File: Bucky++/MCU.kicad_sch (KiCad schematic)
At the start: 38 parts, among them J15 502585-0470, J16 FTSH-105-01-F-D-RA-K, J1702 505110-3091, J1801 S2B-PH-SM4-TB, J403 USB4105-GF-A, Q1401 PMV90ENER, U1 STM32G483RET6, U1801 DGD0216WT-7, Y201 ABM8W-48.0000MHZ-4-D1X-T3

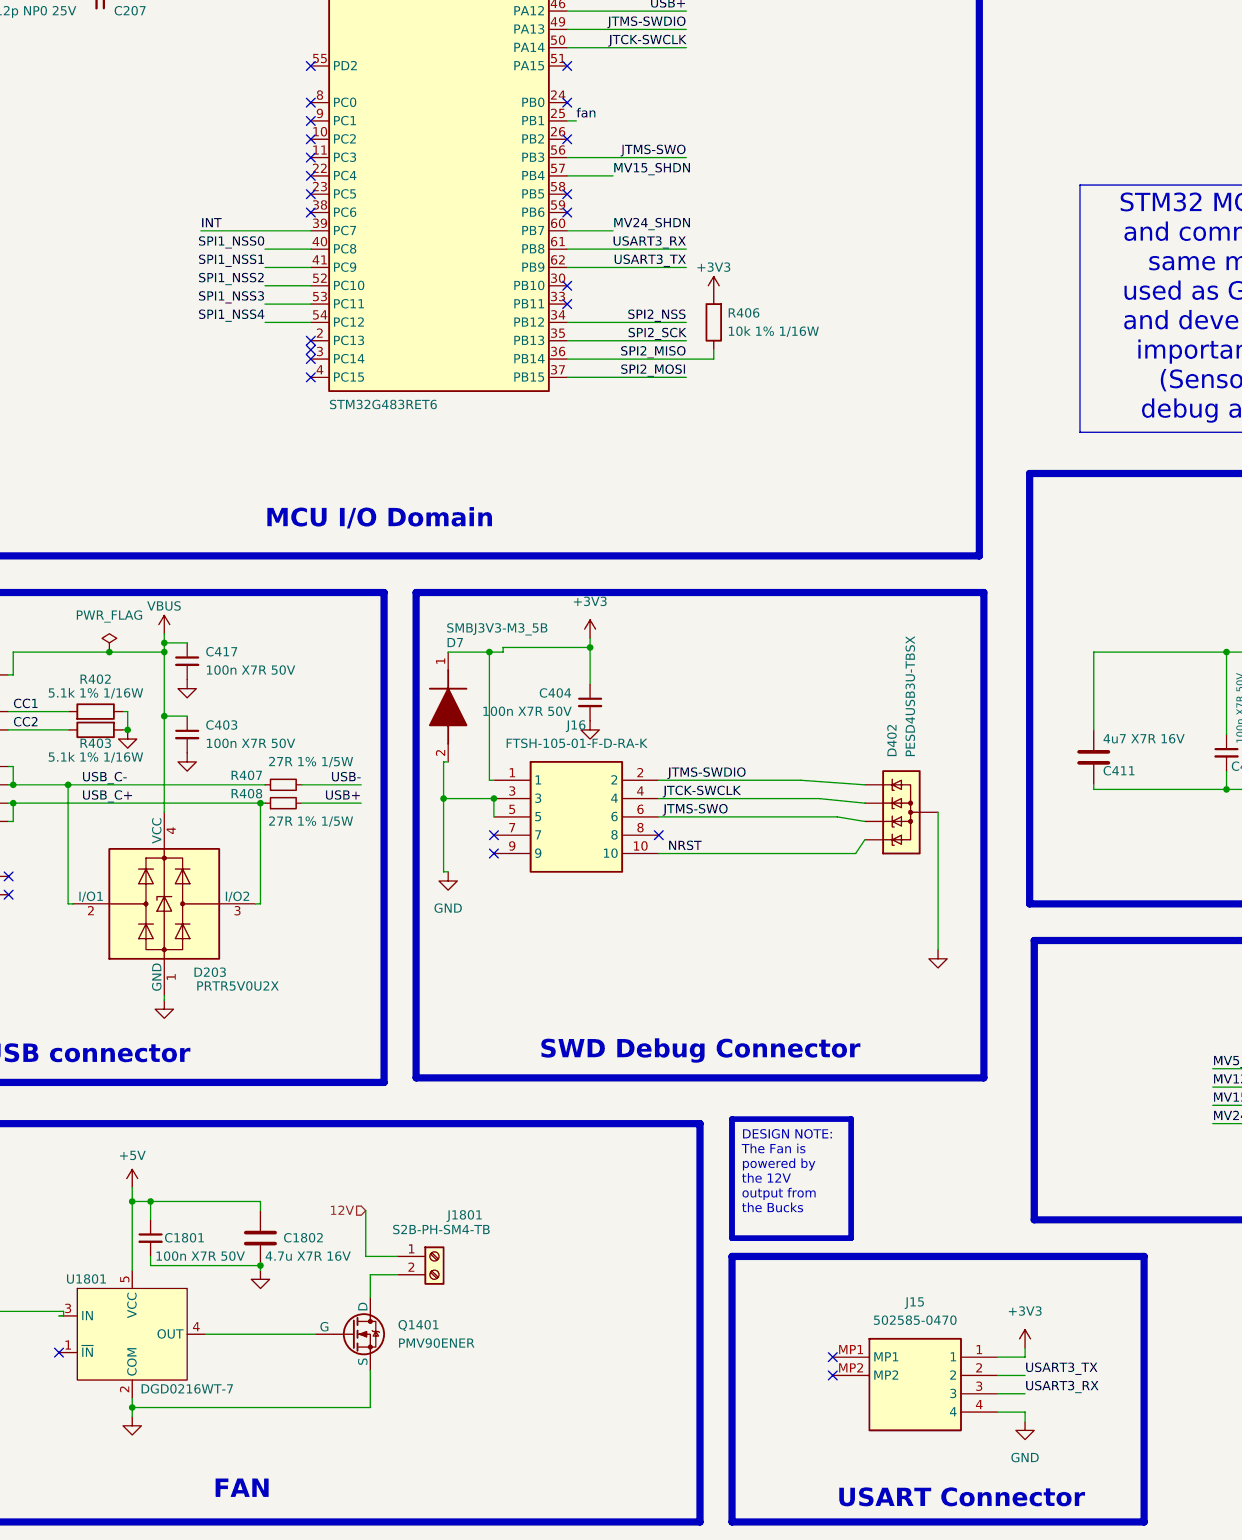
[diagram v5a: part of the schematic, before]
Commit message: updated circuit after review. updated silkscreen
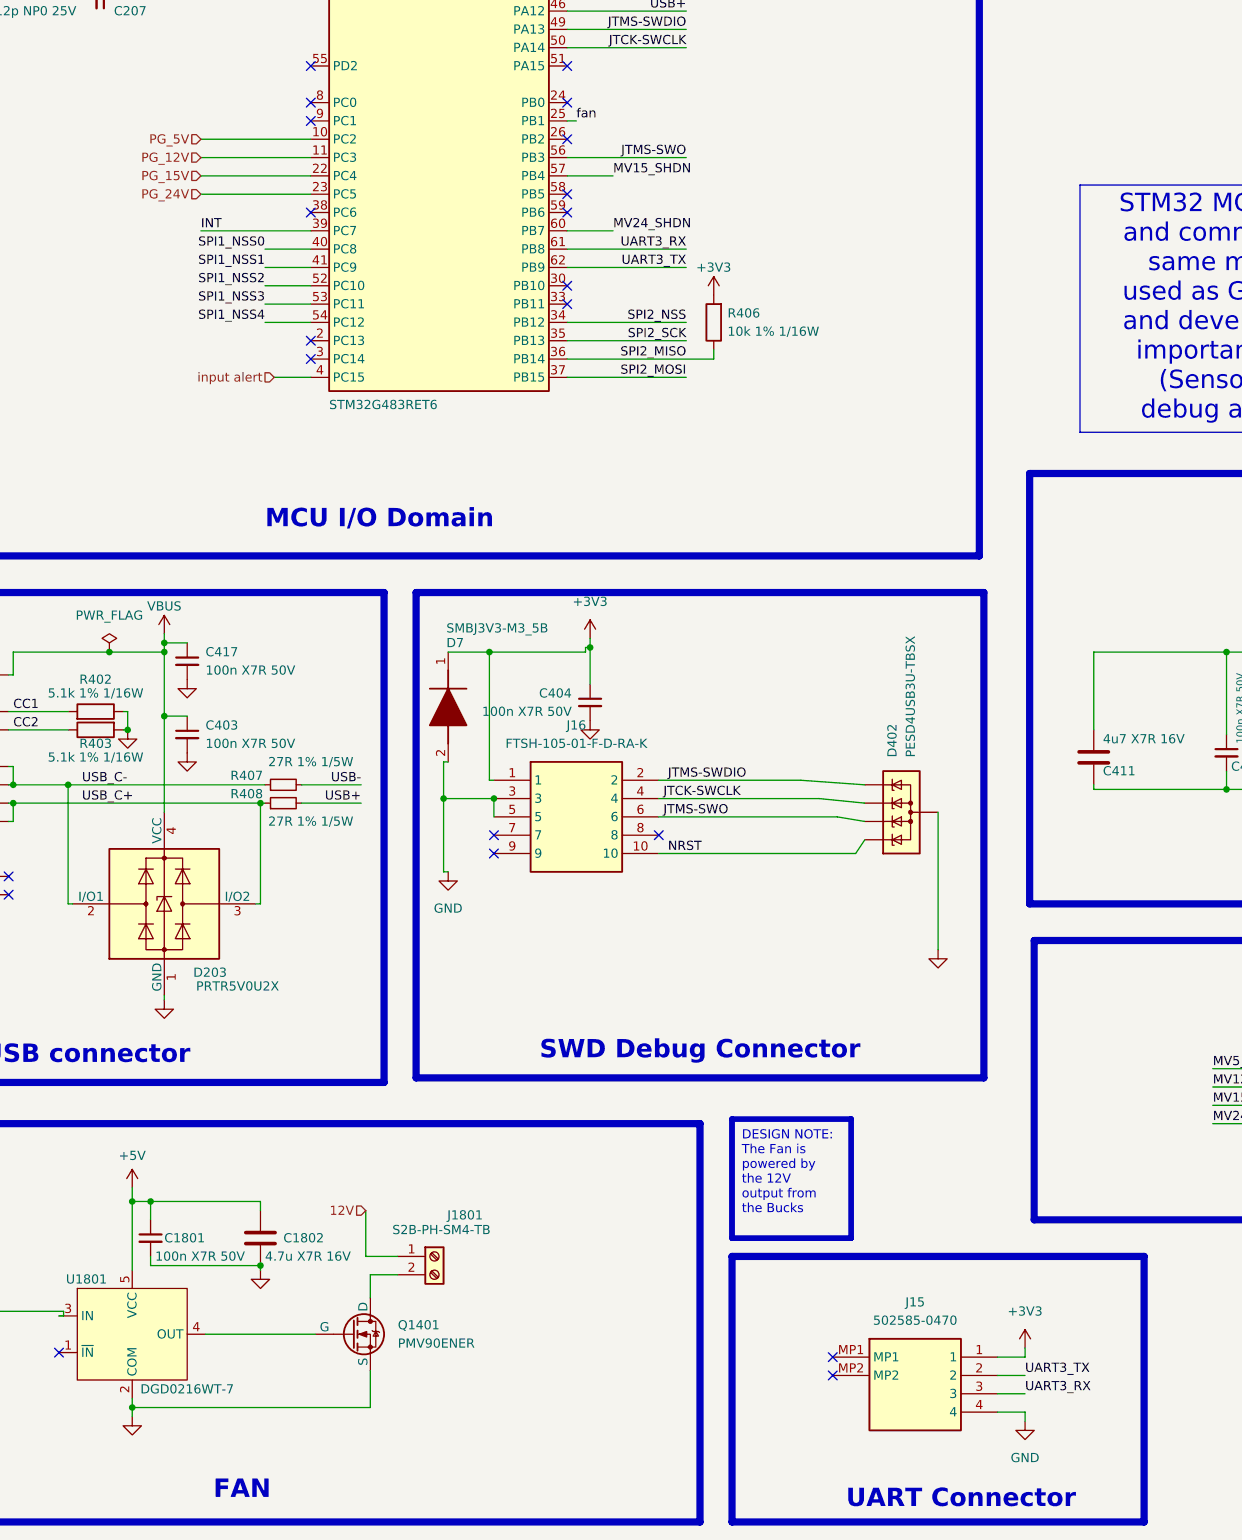
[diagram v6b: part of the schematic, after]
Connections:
- net PG_5V: now reaches U1.10 (PC2)
- net PG_12V: now reaches U1.11 (PC3)
- net PG_15V: now reaches U1.22 (PC4)
- net PG_24V: now reaches U1.23 (PC5)
- net input alert: now reaches U1.4 (PC15)
- net USART3_RX renamed UART3_RX
- net USART3_TX renamed UART3_TX
- no-connect marks 47 -> 41
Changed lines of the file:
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@@
 		)
 	)
-	(text_box "USART Connector"
+	(text_box "UART Connector"
 		(exclude_from_sim no)
 		(at 157.48 271.145 0)
@@
 	)
 	(no_connect
-		(at 91.44 93.98)
-	)
-	(no_connect
-		(at 91.44 119.38)
-	)
-	(no_connect
 		(at 321.31 48.26)
 	)
@@
 	)
 	(no_connect
-		(at 91.44 86.36)
-	)
-	(no_connect
-		(at 91.44 88.9)
-	)
-	(no_connect
 		(at 133.35 43.18)
 	)
 	(no_connect
-		(at 91.44 115.57)
-	)
-	(no_connect
 		(at 91.44 76.2)
 	)
@@
 	)
 	(no_connect
-		(at 91.44 91.44)
-	)
-	(no_connect
 		(at 116.84 185.42)
 	)
@@
 	(wire
 		(pts
-			(xy 118.11 156.845) (xy 118.11 157.48)
+			(xy 49.53 48.895) (xy 49.53 57.785)
 		)
 		(stroke
@@
 	(wire
 		(pts
-			(xy 49.53 48.895) (xy 49.53 57.785)
+			(xy 267.97 176.53) (xy 280.67 176.53)
 		)
 		(stroke
@@
 	(wire
 		(pts
-			(xy 267.97 176.53) (xy 280.67 176.53)
+			(xy 318.135 161.29) (xy 318.135 158.75)
 		)
 		(stroke
@@
 	(wire
 		(pts
-			(xy 318.135 161.29) (xy 318.135 158.75)
+			(xy 305.435 173.99) (xy 305.435 176.53)
 		)
 		(stroke
@@
 	(wire
 		(pts
-			(xy 305.435 173.99) (xy 305.435 176.53)
+			(xy 76.2 86.36) (xy 91.44 86.36)
 		)
 		(stroke
@@
 	(wire
 		(pts
+			(xy 76.2 93.98) (xy 91.44 93.98)
+		)
+		(stroke
+			(width 0)
+			(type default)
+		)
+	)
+	(wire
+		(pts
 			(xy 311.785 96.52) (xy 321.31 96.52)
 		)
@@
 	(wire
 		(pts
+			(xy 76.2 91.44) (xy 91.44 91.44)
+		)
+		(stroke
+			(width 0)
+			(type default)
+		)
+	)
+	(wire
+		(pts
+			(xy 86.36 119.38) (xy 91.44 119.38)
+		)
+		(stroke
+			(width 0)
+			(type default)
+		)
+	)
+	(wire
+		(pts
 			(xy 65.405 168.275) (xy 66.04 168.275)
 		)
@@
 	(wire
 		(pts
-			(xy 118.11 156.845) (xy 130.175 156.845)
-		)
-		(stroke
-			(width 0)
-			(type default)
-		)
-	)
-	(wire
-		(pts
 			(xy 133.35 40.64) (xy 127 40.64)
 		)
@@
 	(wire
 		(pts
+			(xy 129.54 156.845) (xy 130.175 156.845)
+		)
+		(stroke
+			(width 0)
+			(type default)
+		)
+	)
+	(wire
+		(pts
 			(xy 311.785 45.72) (xy 321.31 45.72)
 		)
@@
 	(wire
 		(pts
+			(xy 76.2 88.9) (xy 91.44 88.9)
+		)
+		(stroke
+			(width 0)
+			(type default)
+		)
+	)
+	(wire
+		(pts
 			(xy 127 68.58) (xy 143.51 68.58)
 		)
@@
 	(wire
 		(pts
-			(xy 118.11 157.48) (xy 116.205 157.48)
+			(xy 116.205 157.48) (xy 129.54 157.48)
 		)
 		(stroke
@@
 	(wire
 		(pts
+			(xy 129.54 157.48) (xy 129.54 156.845)
+		)
+		(stroke
+			(width 0)
+			(type default)
+		)
+	)
+	(wire
+		(pts
 			(xy 216.535 215.265) (xy 226.695 215.265)
 		)
@@
 		)
 	)
-	(label "USART3_RX"
+	(label "UART3_RX"
 		(at 143.51 101.6 180)
 		(effects
@@
 		)
 	)
-	(label "USART3_TX"
+	(label "UART3_TX"
 		(at 190.5 257.81 0)
 		(effects
@@
 		)
 	)
-	(label "USART3_TX"
+	(label "UART3_TX"
 		(at 143.51 104.14 180)
 		(effects
@@
 		)
 	)
-	(label "USART3_RX"
+	(label "UART3_RX"
 		(at 190.5 260.35 0)
 		(effects
@@
 		)
 	)
+	(hierarchical_label "PG_24V"
+		(shape input)
+		(at 76.2 93.98 180)
+		(effects
+			(font
+				(size 1.27 1.27)
+			)
+			(justify right)
+		)
+	)
+	(hierarchical_label "PG_15V"
+		(shape input)
+		(at 76.2 91.44 180)
+		(effects
+			(font
+				(size 1.27 1.27)
+			)
+			(justify right)
+		)
+	)
 	(hierarchical_label "{SPI_BAT}"
 		(shape bidirectional)
@@
 		)
 	)
+	(hierarchical_label "PG_12V"
+		(shape input)
+		(at 76.2 88.9 180)
+		(effects
+			(font
+				(size 1.27 1.27)
+			)
+			(justify right)
+		)
+	)
+	(hierarchical_label "PG_5V"
+		(shape input)
+		(at 76.2 86.36 180)
+		(effects
+			(font
+				(size 1.27 1.27)
+			)
+			(justify right)
+		)
+	)
+	(hierarchical_label "input alert"
+		(shape input)
+		(at 86.36 119.38 180)
+		(effects
+			(font
+				(size 1.27 1.27)
+			)
+			(justify right)
+		)
+	)

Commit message: fixed second review comment
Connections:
- net GND: now also J15.MP1, J15.MP2, J1702.MP1, J1702.MP2
- no-connect marks 41 -> 37
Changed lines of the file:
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@@
 	)
 	(junction
+		(at 163.83 257.81)
+		(diameter 0)
+		(color 0 0 0 0)
+	)
+	(junction
 		(at 318.135 153.67)
 		(diameter 0)
@@
 	)
 	(junction
+		(at 346.71 104.14)
+		(diameter 0)
+		(color 0 0 0 0)
+	)
+	(junction
 		(at 287.02 165.735)
 		(diameter 0)
@@
 	)
 	(no_connect
-		(at 346.71 104.14)
-	)
-	(no_connect
-		(at 346.71 101.6)
-	)
-	(no_connect
 		(at 321.31 81.28)
 	)
@@
 	)
 	(no_connect
-		(at 163.83 257.81)
-	)
-	(no_connect
 		(at 321.31 55.88)
 	)
@@
 		(at 127 86.36)
 	)
-	(no_connect
-		(at 163.83 255.27)
-	)
 	(bus_entry
 		(at 267.97 224.79)
@@
 	(wire
 		(pts
+			(xy 163.83 257.81) (xy 163.83 259.08)
+		)
+		(stroke
+			(width 0)
+			(type default)
+		)
+	)
+	(wire
+		(pts
 			(xy 71.12 166.37) (xy 71.12 179.705)
 		)
@@
 	(wire
 		(pts
+			(xy 163.83 255.27) (xy 163.83 257.81)
+		)
+		(stroke
+			(width 0)
+			(type default)
+		)
+	)
+	(wire
+		(pts
 			(xy 57.785 175.895) (xy 85.09 175.895)
 		)
@@
 	(wire
 		(pts
+			(xy 346.71 101.6) (xy 346.71 104.14)
+		)
+		(stroke
+			(width 0)
+			(type default)
+		)
+	)
+	(wire
+		(pts
 			(xy 129.54 157.48) (xy 129.54 156.845)
 		)
@@
 	)
 	(symbol
+		(lib_name "GND_5")
+		(lib_id "power:GND")
+		(at 163.83 259.08 0)
+		(unit 1)
+		(exclude_from_sim no)
+		(in_bom yes)
+		(on_board yes)
+		(dnp no)
+		(fields_autoplaced yes)
+		(property "Reference" "#PWR0120"
+			(at 163.83 265.43 0)
+			(effects
+				(font
+					(size 1.27 1.27)
+				)
+				(hide yes)
+			)
+		)
+		(property "Value" "GND"
+			(at 163.83 263.525 0)
+			(effects
+				(font
+					(size 1.27 1.27)
+				)
+				(hide yes)
+			)
+		)
+		(property "Footprint" ""
+			(at 163.83 259.08 0)
+			(effects
+				(font
+					(size 1.27 1.27)
+				)
+				(hide yes)
+			)
+		)
+		(property "Datasheet" ""
+			(at 163.83 259.08 0)
+			(effects
+				(font
+					(size 1.27 1.27)
+				)
+				(hide yes)
+			)
+		)
+		(property "Description" ""
+			(at 163.83 259.08 0)
+			(effects
+				(font
+					(size 1.27 1.27)
+				)
+				(hide yes)
+			)
+		)
+		(pin "1"
+		)
+		(instances
+			(project "Bucky++"
+				(path "/0650c7a8-acba-429c-9f8e-eec0baf0bc1c/fede4c36-00cc-4d3d-b71c-5243ba232202/694c70cd-5237-46a2-a5ef-62c4b649ef6f"
+					(reference "#PWR0120")
+					(unit 1)
+				)
+			)
+		)
+	)
+	(symbol
 		(lib_id "Device:R")
 		(at 61.595 168.275 90)
@@
 					(unit 1)
 				)
+			)
+		)
+	)
+	(symbol
+		(lib_name "GND_5")
+		(lib_id "power:GND")
+		(at 346.71 104.14 0)
+		(unit 1)
+		(exclude_from_sim no)
+		(in_bom yes)
+		(on_board yes)
+		(dnp no)
+		(fields_autoplaced yes)
+		(property "Reference" "#PWR0119"
+			(at 346.71 110.49 0)
+			(effects
+				(font
+					(size 1.27 1.27)
+				)
+				(hide yes)
+			)
+		)
+		(property "Value" "GND"
+			(at 346.71 108.585 0)
+			(effects
+				(font
+					(size 1.27 1.27)
+				)
+				(hide yes)
+			)
+		)
+		(property "Footprint" ""
+			(at 346.71 104.14 0)
+			(effects
+				(font
+					(size 1.27 1.27)
+				)
+				(hide yes)
+			)
+		)
+		(property "Datasheet" ""
+			(at 346.71 104.14 0)
+			(effects
+				(font
+					(size 1.27 1.27)
+				)
+				(hide yes)
+			)
+		)
+		(property "Description" ""
+			(at 346.71 104.14 0)
+			(effects
+				(font
+					(size 1.27 1.27)
+				)
+				(hide yes)
+			)
+		)
+		(pin "1"
+		)
+		(instances
+			(project "Bucky++"
+				(path "/0650c7a8-acba-429c-9f8e-eec0baf0bc1c/fede4c36-00cc-4d3d-b71c-5243ba232202/694c70cd-5237-46a2-a5ef-62c4b649ef6f"
+					(reference "#PWR0119")
+					(unit 1)
+				)

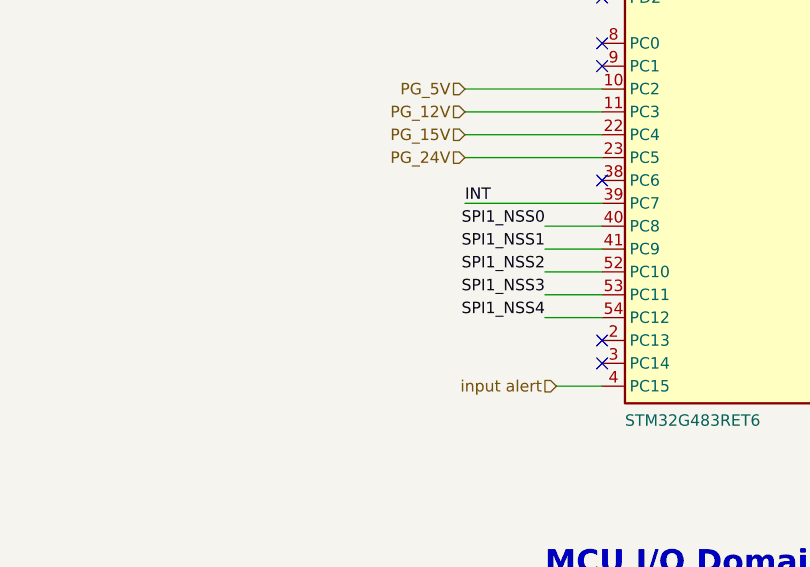
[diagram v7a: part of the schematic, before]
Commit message: fix layout and tolerance issues, started working on routing alerts
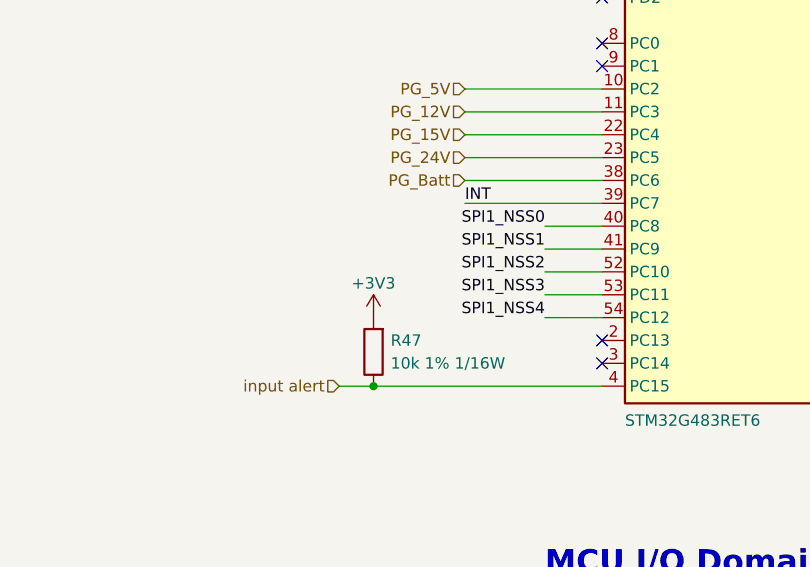
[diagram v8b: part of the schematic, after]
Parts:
- added R47: 10k 1% 1/16W, 0_resistor_smd:R_0402_1005_DensityHigh, symbol Device:R
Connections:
- net +3V3: now also R47.2
- net input alert: now also R47.1
- net PG_Batt: now reaches U1.38 (PC6)
- no-connect marks 37 -> 36
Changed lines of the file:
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@@
 	)
 	(junction
+		(at 66.04 119.38)
+		(diameter 0)
+		(color 0 0 0 0)
+	)
+	(junction
 		(at 66.675 233.68)
 		(diameter 0)
@@
 	)
 	(no_connect
-		(at 91.44 96.52)
-	)
-	(no_connect
 		(at 133.35 40.64)
 	)
@@
 	(wire
 		(pts
-			(xy 86.36 119.38) (xy 91.44 119.38)
+			(xy 62.23 119.38) (xy 66.04 119.38)
 		)
 		(stroke
@@
 	(wire
 		(pts
+			(xy 76.2 96.52) (xy 91.44 96.52)
+		)
+		(stroke
+			(width 0)
+			(type default)
+		)
+	)
+	(wire
+		(pts
 			(xy 50.165 175.895) (xy 57.785 175.895)
 		)
@@
 	(wire
 		(pts
+			(xy 66.04 119.38) (xy 91.44 119.38)
+		)
+		(stroke
+			(width 0)
+			(type default)
+		)
+	)
+	(wire
+		(pts
 			(xy 51.435 57.785) (xy 49.53 57.785)
 		)
@@
 		)
 	)
+	(hierarchical_label "PG_Batt"
+		(shape input)
+		(at 76.2 96.52 180)
+		(effects
+			(font
+				(size 1.27 1.27)
+			)
+			(justify right)
+		)
+	)
 	(hierarchical_label "PG_5V"
 		(shape input)
@@
 	(hierarchical_label "input alert"
 		(shape input)
-		(at 86.36 119.38 180)
+		(at 62.23 119.38 180)
 		(effects
 			(font
@@
 	)
 	(symbol
+		(lib_id "Device:R")
+		(at 66.04 115.57 180)
+		(unit 1)
+		(exclude_from_sim no)
+		(in_bom yes)
+		(on_board yes)
+		(dnp no)
+		(fields_autoplaced yes)
+		(property "Reference" "R47"
+			(at 67.945 114.3 0)
+			(effects
+				(font
+					(size 1.27 1.27)
+				)
+				(justify right)
+			)
+		)
+		(property "Value" "10k 1% 1/16W"
+			(at 67.945 116.84 0)
+			(effects
+				(font
+					(size 1.27 1.27)
+				)
+				(justify right)
+			)
+		)
+		(property "Footprint" "0_resistor_smd:R_0402_1005_DensityHigh"
+			(at 67.818 115.57 90)
+			(effects
+				(font
+					(size 1.27 1.27)
+				)
+				(hide yes)
+			)
+		)
+		(property "Datasheet" "~"
+			(at 66.04 115.57 0)
+			(effects
+				(font
+					(size 1.27 1.27)
+				)
+				(hide yes)
+			)
+		)
+		(property "Description" ""
+			(at 66.04 115.57 0)
+			(effects
+				(font
+					(size 1.27 1.27)
+				)
+				(hide yes)
+			)
+		)
+		(pin "1"
+		)
+		(pin "2"
+		)
+		(instances
+			(project "Bucky++"
+				(path "/0650c7a8-acba-429c-9f8e-eec0baf0bc1c/fede4c36-00cc-4d3d-b71c-5243ba232202/694c70cd-5237-46a2-a5ef-62c4b649ef6f"
+					(reference "R47")
+					(unit 1)
+				)
+			)
+		)
+	)
+	(symbol
 		(lib_id "Device:C_Small")
 		(at 218.44 171.45 0)
@@
 					(unit 1)
 				)
+			)
+		)
+	)
+	(symbol
+		(lib_id "power:+3V3")
+		(at 66.04 111.76 0)
+		(mirror y)
+		(unit 1)
+		(exclude_from_sim no)
+		(in_bom yes)
+		(on_board yes)
+		(dnp no)
+		(property "Reference" "#PWR0121"
+			(at 66.04 115.57 0)
+			(effects
+				(font
+					(size 1.27 1.27)
+				)
+				(hide yes)
+			)
+		)
+		(property "Value" "+3V3"
+			(at 66.04 107.95 0)
+			(effects
+				(font
+					(size 1.27 1.27)
+				)
+			)
+		)
+		(property "Footprint" ""
+			(at 66.04 111.76 0)
+			(effects
+				(font
+					(size 1.27 1.27)
+				)
+				(hide yes)
+			)
+		)
+		(property "Datasheet" ""
+			(at 66.04 111.76 0)
+			(effects
+				(font
+					(size 1.27 1.27)
+				)
+				(hide yes)
+			)
+		)
+		(property "Description" ""
+			(at 66.04 111.76 0)
+			(effects
+				(font
+					(size 1.27 1.27)
+				)
+				(hide yes)
+			)
+		)
+		(pin "1"
+		)
+		(instances
+			(project "Bucky++"
+				(path "/0650c7a8-acba-429c-9f8e-eec0baf0bc1c/fede4c36-00cc-4d3d-b71c-5243ba232202/694c70cd-5237-46a2-a5ef-62c4b649ef6f"
+					(reference "#PWR0121")
+					(unit 1)
+				)
